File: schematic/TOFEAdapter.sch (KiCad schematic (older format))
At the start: 2 parts, among them U1 TOFE-8X, U2 TOFE-8X

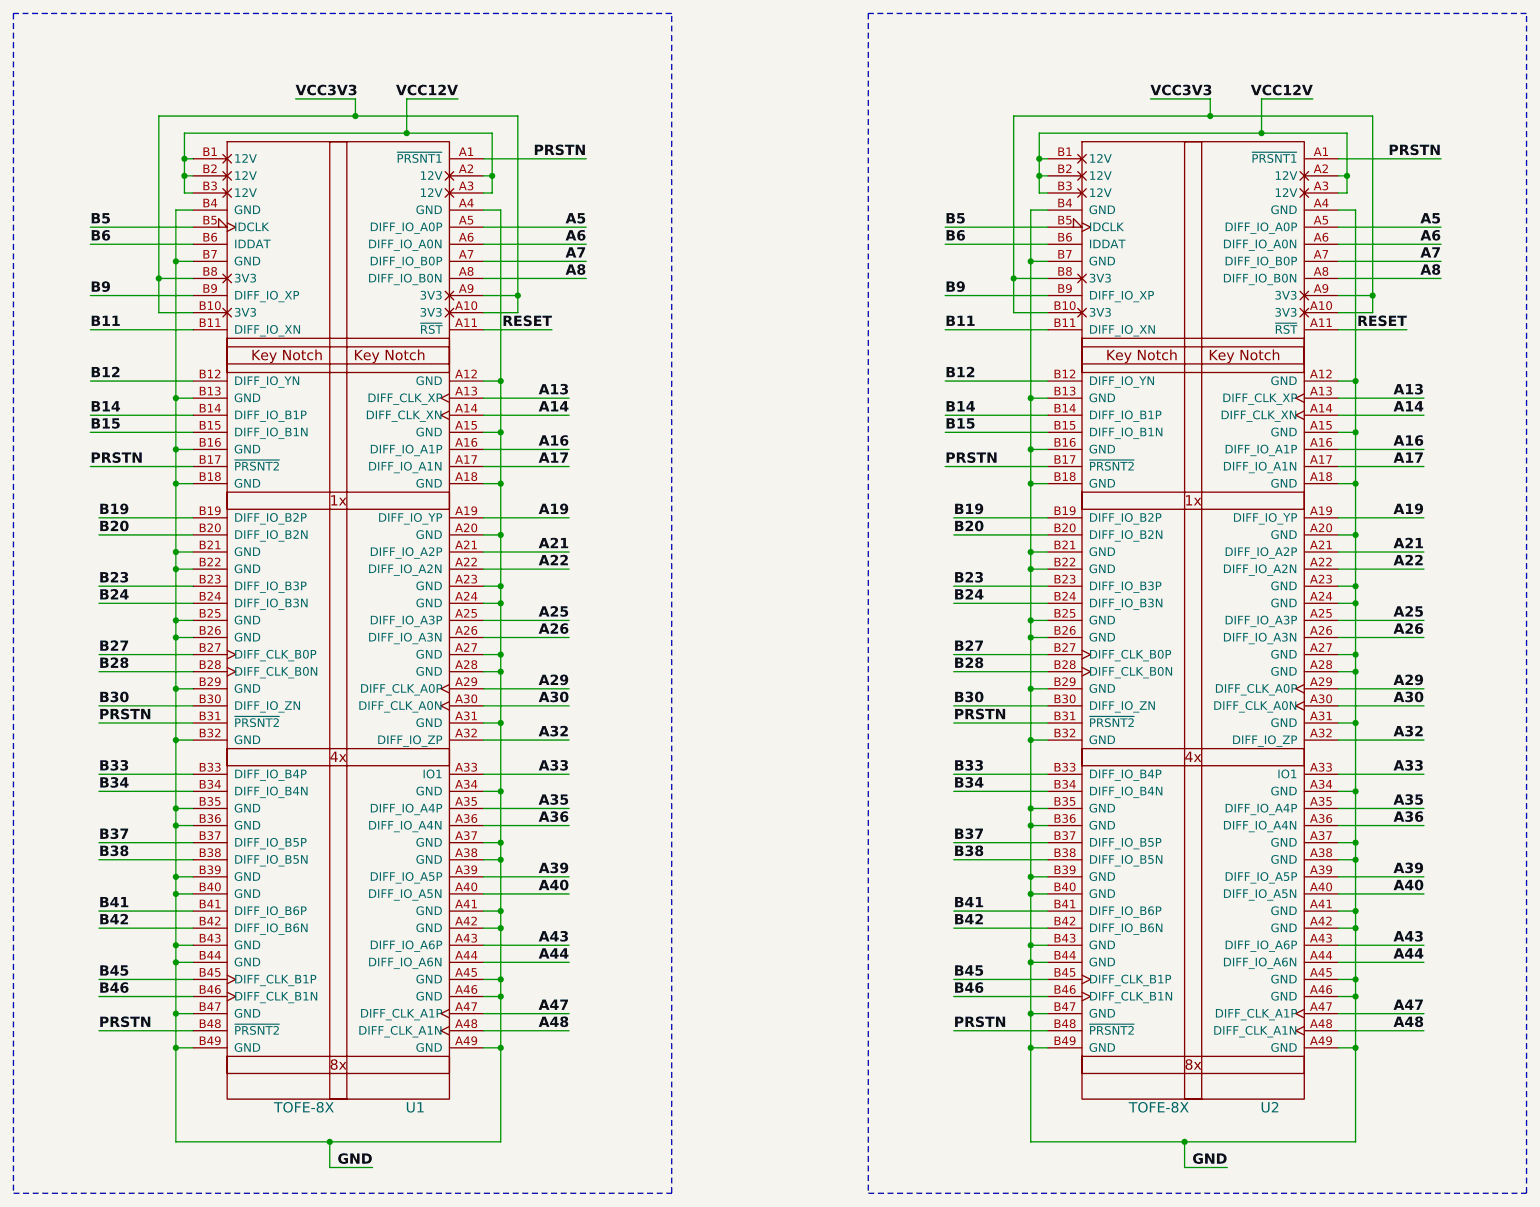
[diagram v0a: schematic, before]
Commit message: Giving the nets names which KiCad understands.
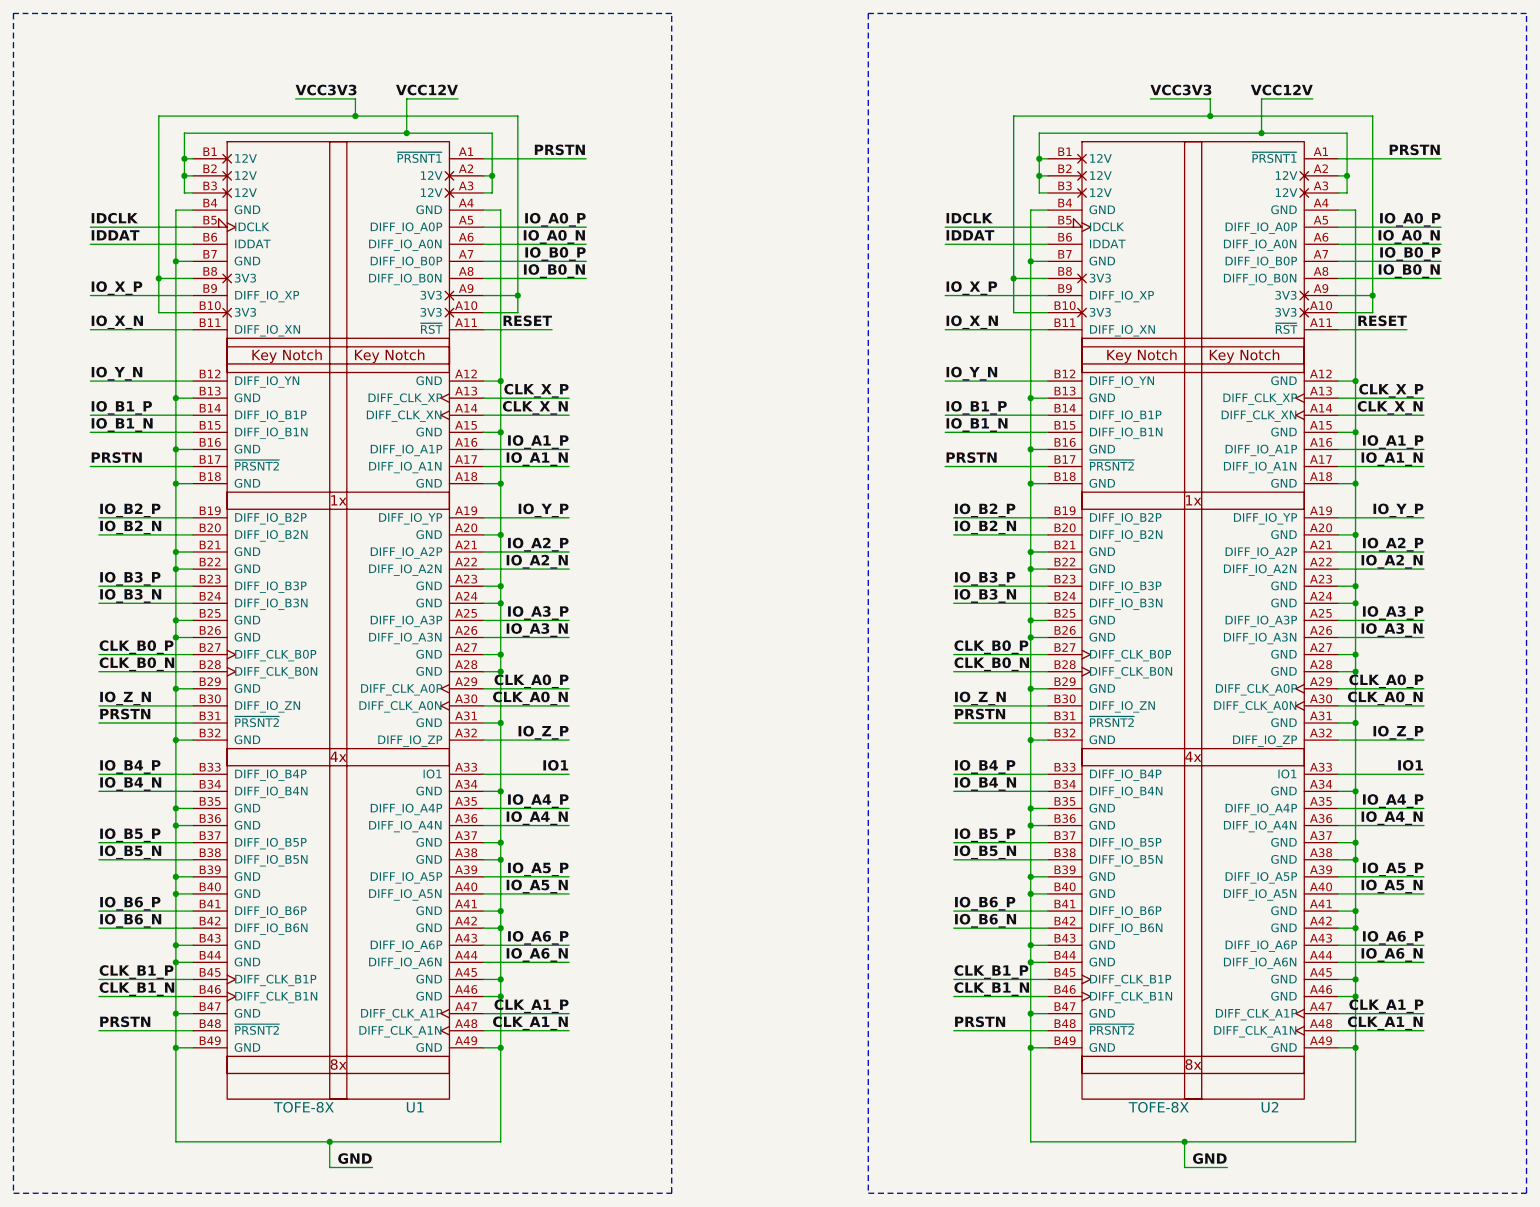
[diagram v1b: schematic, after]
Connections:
- net A13 renamed CLK_X_P
- net A14 renamed CLK_X_N
- net A16 renamed IO_A1_P
- net A17 renamed IO_A1_N
- net A19 renamed IO_Y_P
- net A21 renamed IO_A2_P
- net A22 renamed IO_A2_N
- net A25 renamed IO_A3_P
- net A26 renamed IO_A3_N
- net A29 renamed CLK_A0_P
- net A30 renamed CLK_A0_N
- net A32 renamed IO_Z_P
- net A33 renamed IO1
- net A35 renamed IO_A4_P
- net A36 renamed IO_A4_N
- net A39 renamed IO_A5_P
- net A40 renamed IO_A5_N
- net A43 renamed IO_A6_P
- net A44 renamed IO_A6_N
- net A47 renamed CLK_A1_P
- net A48 renamed CLK_A1_N
- net A5 renamed IO_A0_P
- net A6 renamed IO_A0_N
- net A7 renamed IO_B0_P
- net A8 renamed IO_B0_N
- net B11 renamed IO_X_N
- net B12 renamed IO_Y_N
- net B14 renamed IO_B1_P
- net B15 renamed IO_B1_N
- net B19 renamed IO_B2_P
- net B20 renamed IO_B2_N
- net B23 renamed IO_B3_P
- net B24 renamed IO_B3_N
- net B27 renamed CLK_B0_P
- net B28 renamed CLK_B0_N
- net B30 renamed IO_Z_N
- net B33 renamed IO_B4_P
- net B34 renamed IO_B4_N
- net B37 renamed IO_B5_P
- net B38 renamed IO_B5_N
- net B41 renamed IO_B6_P
- net B42 renamed IO_B6_N
- net B45 renamed CLK_B1_P
- net B46 renamed CLK_B1_N
- net B5 renamed IDCLK
- net B6 renamed IDDAT
- net B9 renamed IO_X_P
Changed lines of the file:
@@
 GND
 Text Label 6200 2950 2    60   ~ 12
-A5
+IO_A0_P
 Text Label 6200 3050 2    60   ~ 12
-A6
+IO_A0_N
 Text Label 6200 3150 2    60   ~ 12
-A7
+IO_B0_P
 Text Label 6200 3250 2    60   ~ 12
-A8
+IO_B0_N
 Text Label 6100 3950 2    60   ~ 12
-A13
+CLK_X_P
 Text Label 6100 4050 2    60   ~ 12
-A14
+CLK_X_N
 Text Label 6100 4250 2    60   ~ 12
-A16
+IO_A1_P
 Text Label 6100 4350 2    60   ~ 12
-A17
+IO_A1_N
 Text Label 6100 4850 2    60   ~ 12
-A21
+IO_A2_P
 Text Label 6100 4950 2    60   ~ 12
-A22
+IO_A2_N
 Text Label 6100 5250 2    60   ~ 12
-A25
+IO_A3_P
 Text Label 6100 5350 2    60   ~ 12
-A26
+IO_A3_N
 Text Label 6100 5650 2    60   ~ 12
-A29
+CLK_A0_P
 Text Label 6100 5750 2    60   ~ 12
-A30
+CLK_A0_N
 Text Label 6100 6350 2    60   ~ 12
-A35
+IO_A4_P
 Text Label 4500 2200 0    60   ~ 12
 VCC3V3
@@
 VCC12V
 Text Label 3300 4050 0    60   ~ 12
-B14
+IO_B1_P
 Text Label 3300 4150 0    60   ~ 12
-B15
+IO_B1_N
 Text Label 3350 4650 0    60   ~ 12
-B19
+IO_B2_P
 Text Label 3350 4750 0    60   ~ 12
-B20
+IO_B2_N
 Text Label 6100 4650 2    60   ~ 12
-A19
+IO_Y_P
 Text Label 3350 5150 0    60   ~ 12
-B24
+IO_B3_N
 Text Label 3350 5050 0    60   ~ 12
-B23
+IO_B3_P
 Text Label 3350 5550 0    60   ~ 12
-B28
+CLK_B0_N
 Text Label 3350 5450 0    60   ~ 12
-B27
+CLK_B0_P
 Text Label 3350 5750 0    60   ~ 12
-B30
+IO_Z_N
 Text Label 6100 5950 2    60   ~ 12
-A32
+IO_Z_P
 Text Label 3350 6250 0    60   ~ 12
-B34
+IO_B4_N
 Text Label 3350 6150 0    60   ~ 12
-B33
+IO_B4_P
 Text Label 3350 6650 0    60   ~ 12
-B38
+IO_B5_N
 Text Label 3350 6950 0    60   ~ 12
-B41
+IO_B6_P
 Text Label 6100 6750 2    60   ~ 12
-A39
+IO_A5_P
 Text Label 6100 6850 2    60   ~ 12
-A40
+IO_A5_N
 Text Label 6100 7250 2    60   ~ 12
-A44
+IO_A6_N
 Text Label 3350 7350 0    60   ~ 12
-B45
+CLK_B1_P
 Text Label 3300 3850 0    60   ~ 12
-B12
+IO_Y_N
 Text Label 6100 6450 2    60   ~ 12
-A36
+IO_A4_N
 Text Label 6000 3550 2    60   ~ 12
 RESET
 Text Label 3350 6550 0    60   ~ 12
-B37
+IO_B5_P
 Text Label 6100 7650 2    60   ~ 12
-A48
+CLK_A1_N
 Text Label 3350 7050 0    60   ~ 12
-B42
+IO_B6_N
 Text Label 3350 7450 0    60   ~ 12
-B46
+CLK_B1_N
 Text Label 3300 3050 0    60   ~ 12
-B6
+IDDAT
 Text Label 3300 2950 0    60   ~ 12
-B5
+IDCLK
 Text Label 3300 3350 0    60   ~ 12
-B9
+IO_X_P
 Text Label 3300 3550 0    60   ~ 12
-B11
+IO_X_N
 Text Label 6100 7550 2    60   ~ 12
-A47
+CLK_A1_P
 Text Label 6100 7150 2    60   ~ 12
-A43
+IO_A6_P
 Wire Wire Line
 	3900 2850 3800 2850
@@
 	6200 2550 5600 2550
 Text Label 6100 6150 2    60   ~ 12
-A33
+IO1
 Wire Wire Line
 	5600 6150 6100 6150
@@
 GND
 Text Label 11200 2950 2    60   ~ 12
-A5
+IO_A0_P
 Text Label 11200 3050 2    60   ~ 12
-A6
+IO_A0_N
 Text Label 11200 3150 2    60   ~ 12
-A7
+IO_B0_P
 Text Label 11200 3250 2    60   ~ 12
-A8
+IO_B0_N
 Text Label 11100 3950 2    60   ~ 12
-A13
+CLK_X_P
 Text Label 11100 4050 2    60   ~ 12
-A14
+CLK_X_N
 Text Label 11100 4250 2    60   ~ 12
-A16
+IO_A1_P
 Text Label 11100 4350 2    60   ~ 12
-A17
+IO_A1_N
 Text Label 11100 4850 2    60   ~ 12
-A21
+IO_A2_P
 Text Label 11100 4950 2    60   ~ 12
-A22
+IO_A2_N
 Text Label 11100 5250 2    60   ~ 12
-A25
+IO_A3_P
 Text Label 11100 5350 2    60   ~ 12
-A26
+IO_A3_N
 Text Label 11100 5650 2    60   ~ 12
-A29
+CLK_A0_P
 Text Label 11100 5750 2    60   ~ 12
-A30
+CLK_A0_N
 Text Label 11100 6350 2    60   ~ 12
-A35
+IO_A4_P
 Text Label 9500 2200 0    60   ~ 12
 VCC3V3
 Text Label 8300 4050 0    60   ~ 12
-B14
+IO_B1_P
 Text Label 8300 4150 0    60   ~ 12
-B15
+IO_B1_N
 Text Label 8350 4650 0    60   ~ 12
-B19
+IO_B2_P
 Text Label 8350 4750 0    60   ~ 12
-B20
+IO_B2_N
 Text Label 11100 4650 2    60   ~ 12
-A19
+IO_Y_P
 Text Label 8350 5150 0    60   ~ 12
-B24
+IO_B3_N
 Text Label 8350 5050 0    60   ~ 12
-B23
+IO_B3_P
 Text Label 8350 5550 0    60   ~ 12
-B28
+CLK_B0_N
 Text Label 8350 5450 0    60   ~ 12
-B27
+CLK_B0_P
 Text Label 8350 5750 0    60   ~ 12
-B30
+IO_Z_N
 Text Label 11100 5950 2    60   ~ 12
-A32
+IO_Z_P
 Text Label 8350 6250 0    60   ~ 12
-B34
+IO_B4_N
 Text Label 8350 6150 0    60   ~ 12
-B33
+IO_B4_P
 Text Label 8350 6650 0    60   ~ 12
-B38
+IO_B5_N
 Text Label 8350 6950 0    60   ~ 12
-B41
+IO_B6_P
 Text Label 11100 6750 2    60   ~ 12
-A39
+IO_A5_P
 Text Label 11100 6850 2    60   ~ 12
-A40
+IO_A5_N
 Text Label 11100 7250 2    60   ~ 12
-A44
+IO_A6_N
 Text Label 8350 7350 0    60   ~ 12
-B45
+CLK_B1_P
 Text Label 8300 3850 0    60   ~ 12
-B12
+IO_Y_N
 Text Label 11100 6450 2    60   ~ 12
-A36
+IO_A4_N
 Text Label 11000 3550 2    60   ~ 12
 RESET
 Text Label 8350 6550 0    60   ~ 12
-B37
+IO_B5_P
 Text Label 11100 7650 2    60   ~ 12
-A48
+CLK_A1_N
 Text Label 8350 7050 0    60   ~ 12
-B42
+IO_B6_N
 Text Label 8350 7450 0    60   ~ 12
-B46
+CLK_B1_N
 Text Label 8300 3050 0    60   ~ 12
-B6
+IDDAT
 Text Label 8300 2950 0    60   ~ 12
-B5
+IDCLK
 Text Label 8300 3350 0    60   ~ 12
-B9
+IO_X_P
 Text Label 8300 3550 0    60   ~ 12
-B11
+IO_X_N
 Text Label 11100 7550 2    60   ~ 12
-A47
+CLK_A1_P
 Text Label 11100 7150 2    60   ~ 12
-A43
+IO_A6_P
 Wire Wire Line
 	8900 2850 8800 2850
@@
 	11200 2550 10600 2550
 Text Label 11100 6150 2    60   ~ 12
-A33
+IO1
 Wire Wire Line
 	10600 6150 11100 6150
